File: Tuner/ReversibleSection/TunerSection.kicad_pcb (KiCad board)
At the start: 2 copper layers, 100 x 100 mm, 80 parts, among them J1 Conn_01x03, J10 Conn_01x02, J11 Conn_01x05, J12 Conn_01x01, J13 Conn_01x01, J14 Conn_01x01, J15 Conn_01x01, J2 Conn_01x03, J3 Conn_01x03, J4 Conn_01x03, J5 Conn_01x03, J6 Conn_01x03, J7 Conn_01x03, J8 Conn_01x02, J9 Conn_01x02, P1 Conn_01x01, P10 Conn_01x01, P11 Conn_01x01, P12 Conn_01x01, P2 Conn_01x01, P3 Conn_01x01, P4 Conn_01x01, P5 Conn_01x01, P6 Conn_01x01, P7 Conn_01x01, P8 Conn_01x01, P9 Conn_01x01, U1 MCP23008, U2 ULN2803A

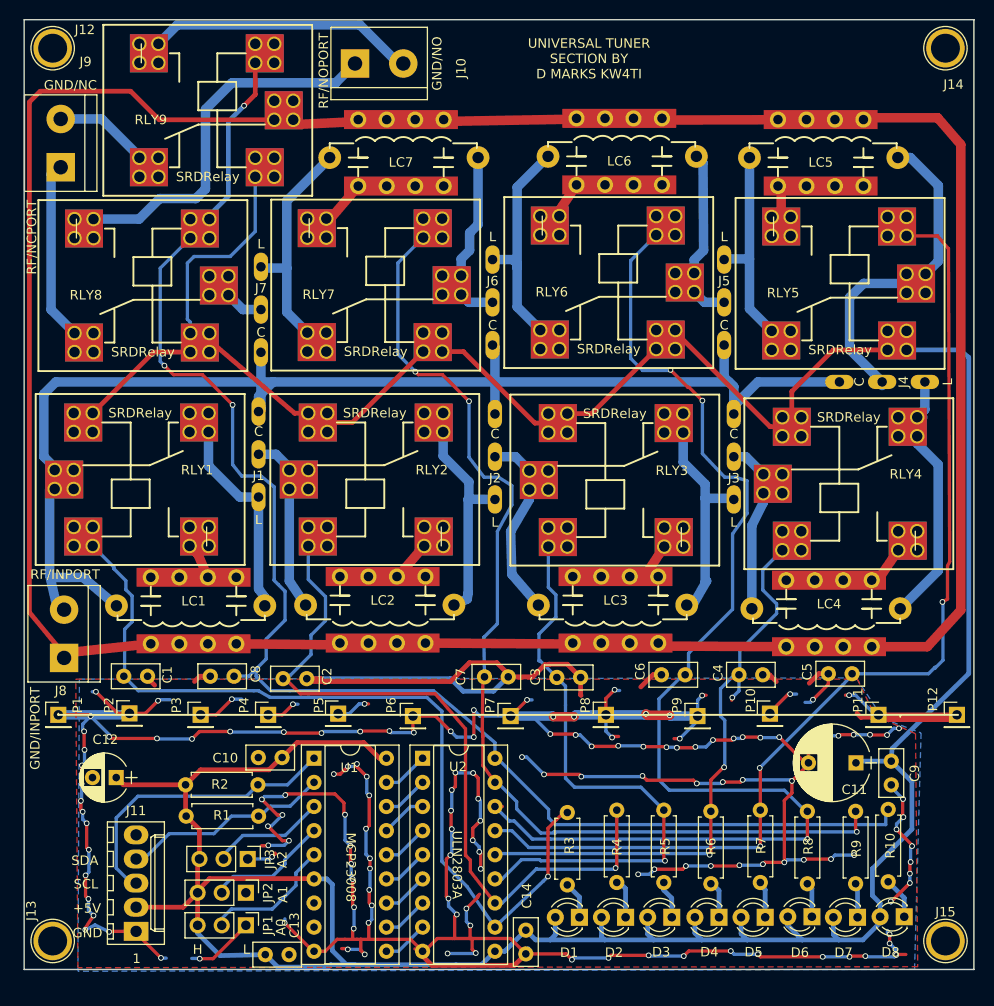
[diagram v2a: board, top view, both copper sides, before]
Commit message: Modified RelayControl and Reversible Section to Isolate Digital from Analog sections using RF chokes
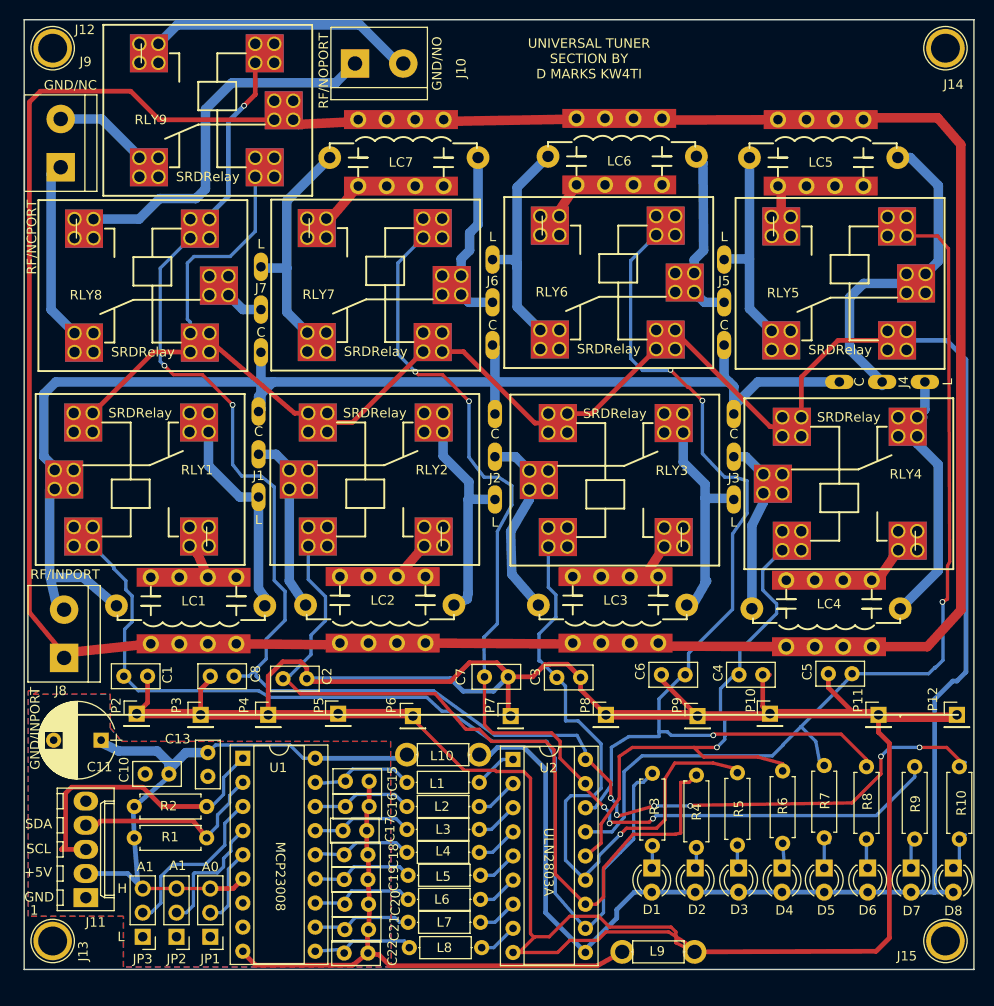
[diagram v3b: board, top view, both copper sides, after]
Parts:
- removed C12: 22 uF, Capacitors_THT:CP_Radial_D5.0mm_P2.50mm
- removed C14, C9: 100 nF, Capacitors_THT:C_Disc_D5.0mm_W2.5mm_P2.50mm
- removed P1: Conn_01x01, Pin_Headers:Pin_Header_Straight_1x01_Pitch2.54mm
- added C15: 10 nF, Capacitors_THT:C_Disc_D5.0mm_W2.5mm_P2.50mm, F.Cu at (83.8, 130.2)
- added C16: C_Small, Capacitors_THT:C_Disc_D5.0mm_W2.5mm_P2.50mm, F.Cu at (83.8, 132.8)
- added C17: C_Small, Capacitors_THT:C_Disc_D5.0mm_W2.5mm_P2.50mm, F.Cu at (83.6, 135.4)
- added C18: 10 nF, Capacitors_THT:C_Disc_D5.0mm_W2.5mm_P2.50mm, F.Cu at (83.7, 137.9)
- added C19: 10 nF, Capacitors_THT:C_Disc_D5.0mm_W2.5mm_P2.50mm, F.Cu at (83.7, 140.5)
- added C20: 10 nF, Capacitors_THT:C_Disc_D5.0mm_W2.5mm_P2.50mm, F.Cu at (83.8, 143.1)
- added C21: 10 nF, Capacitors_THT:C_Disc_D5.0mm_W2.5mm_P2.50mm, F.Cu at (83.8, 145.8)
- added C22: 10 nFl, Capacitors_THT:C_Disc_D5.0mm_W2.5mm_P2.50mm, F.Cu at (83.7, 148.3)
- added L1: 100 uH, Inductors_THT:L_Axial_L5.3mm_D2.2mm_P7.62mm_Horizontal_Vishay_IM-1, F.Cu at (90.3, 130.3)
- added L10: 100 uH, Inductors_THT:L_Axial_L5.3mm_D2.2mm_P7.62mm_Horizontal_Vishay_IM-1, F.Cu at (90.3, 127.4)
- added L2: 100 uH, Inductors_THT:L_Axial_L5.3mm_D2.2mm_P7.62mm_Horizontal_Vishay_IM-1, F.Cu at (90.3, 132.8)
- added L3: 100 uH, Inductors_THT:L_Axial_L5.3mm_D2.2mm_P7.62mm_Horizontal_Vishay_IM-1, F.Cu at (90.3, 135.3)
- added L4: 100 uH, Inductors_THT:L_Axial_L5.3mm_D2.2mm_P7.62mm_Horizontal_Vishay_IM-1, F.Cu at (90.3, 137.7)
- added L5: 100 uH, Inductors_THT:L_Axial_L5.3mm_D2.2mm_P7.62mm_Horizontal_Vishay_IM-1, F.Cu at (90.4, 140.1)
- added L6: 100 uH, Inductors_THT:L_Axial_L5.3mm_D2.2mm_P7.62mm_Horizontal_Vishay_IM-1, F.Cu at (90.4, 142.6)
- added L7: 100 uH, Inductors_THT:L_Axial_L5.3mm_D2.2mm_P7.62mm_Horizontal_Vishay_IM-1, F.Cu at (90.4, 145.0)
- added L8: 100 uH, Inductors_THT:L_Axial_L5.3mm_D2.2mm_P7.62mm_Horizontal_Vishay_IM-1, F.Cu at (90.6, 147.7)
- added L9: 100 uH, Inductors_THT:L_Axial_L5.3mm_D2.2mm_P7.62mm_Horizontal_Vishay_IM-1, F.Cu at (113.0, 148.1)
- moved C11 79.5 mm to (58.1, 125.9)
- moved C13 20.6 mm to (69.3, 129.7), turned to 90 degrees
- moved JP3 13.8 mm to (62.5, 146.6), turned to 180 degrees
- moved C10 12.0 mm to (62.7, 129.4)
- moved R3 9.86 mm to (116.1, 137.0)
- moved U2 9.53 mm to (101.5, 127.9)
- moved D1 9.21 mm to (116.1, 139.3), turned to 270 degrees
- moved R4 9.16 mm to (120.8, 137.2)
- moved D2 8.98 mm to (120.7, 139.3), turned to 270 degrees
- moved D3 8.74 mm to (125.2, 139.3), turned to 270 degrees
- moved R10 8.74 mm to (148.5, 136.3)
- moved R5 8.69 mm to (125.1, 136.9)
- moved R6 8.67 mm to (129.9, 136.7)
- moved JP2 8.65 mm to (66.0, 146.6), turned to 180 degrees
- moved D4 8.42 mm to (129.8, 139.3), turned to 270 degrees
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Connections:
- C1 pad 1: GND -> RLYGND
- C2 pad 1: GND -> RLYGND
- C3 pad 1: GND -> RLYGND
- C4 pad 1: GND -> RLYGND
- C5 pad 1: GND -> RLYGND
- C6 pad 1: GND -> RLYGND
- C7 pad 1: GND -> RLYGND
- C8 pad 1: GND -> RLYGND
- D1 pad 2: +5V -> RLYPWR
- D2 pad 2: +5V -> RLYPWR
- D3 pad 2: +5V -> RLYPWR
- D4 pad 2: +5V -> RLYPWR
- D5 pad 2: +5V -> RLYPWR
- D6 pad 2: +5V -> RLYPWR
- D7 pad 2: +5V -> RLYPWR
- D8 pad 2: +5V -> RLYPWR
- P10 pad 1: GND -> RLYGND
- P11 pad 1: GND -> RLYGND
- P12 pad 1: GND -> RLYGND
- P2 pad 1: GND -> RLYGND
- P3 pad 1: GND -> RLYGND
- P4 pad 1: GND -> RLYGND
- P5 pad 1: GND -> RLYGND
- P6 pad 1: GND -> RLYGND
- P7 pad 1: GND -> RLYGND
- P8 pad 1: GND -> RLYGND
- P9 pad 1: GND -> RLYGND
- RLY1 pad 4: +5V -> RLYPWR
- RLY2 pad 4: +5V -> RLYPWR
- RLY3 pad 4: +5V -> RLYPWR
- RLY4 pad 4: +5V -> RLYPWR
- RLY5 pad 4: +5V -> RLYPWR
- RLY6 pad 4: +5V -> RLYPWR
- RLY7 pad 4: +5V -> RLYPWR
- RLY8 pad 4: +5V -> RLYPWR
- RLY9 pad 4: +5V -> RLYPWR
- U1 pad 10: Net-(U1-Pad10) -> Net-(C22-Pad1)
- U1 pad 11: Net-(U1-Pad11) -> Net-(C21-Pad1)
- U1 pad 12: Net-(U1-Pad12) -> Net-(C20-Pad1)
- U1 pad 13: Net-(U1-Pad13) -> Net-(C19-Pad1)
- U1 pad 14: Net-(U1-Pad14) -> Net-(C18-Pad1)
- U1 pad 15: Net-(U1-Pad15) -> Net-(C17-Pad1)
- U1 pad 16: Net-(U1-Pad16) -> Net-(C16-Pad1)
- U1 pad 17: Net-(U1-Pad17) -> Net-(C15-Pad1)
- U2 pad 1: Net-(U1-Pad17) -> Net-(L1-Pad2)
- U2 pad 10: +5V -> RLYPWR
- U2 pad 2: Net-(U1-Pad16) -> Net-(L2-Pad2)
- U2 pad 3: Net-(U1-Pad15) -> Net-(L3-Pad2)
- U2 pad 4: Net-(U1-Pad14) -> Net-(L4-Pad2)
- U2 pad 5: Net-(U1-Pad13) -> Net-(L5-Pad2)
- U2 pad 6: Net-(U1-Pad12) -> Net-(L6-Pad2)
- U2 pad 7: Net-(U1-Pad11) -> Net-(L7-Pad2)
- U2 pad 8: Net-(U1-Pad10) -> Net-(L8-Pad2)
- U2 pad 9: GND -> RLYGND
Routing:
- net GND: track 577.1 -> 60.4 mm, vias 146 -> 0
- net +5V: track 378.0 -> 69.1 mm
- net RLYGND: track 0.00 -> 291.9 mm
- net RLYPWR: track 0.00 -> 263.1 mm
- net RLY6: track 125.4 -> 102.8 mm
- net RLY1: track 91.4 -> 103.5 mm, vias 1 -> 0
- net Net-(C22-Pad1): track 0.00 -> 11.1 mm
- net Net-(C15-Pad1): track 0.00 -> 11.1 mm
- net Net-(C20-Pad1): track 0.00 -> 11.1 mm
- net RLY8: track 155.0 -> 166.0 mm, vias 3 -> 9
- net Net-(C19-Pad1): track 0.00 -> 10.8 mm
- net Net-(C17-Pad1): track 0.00 -> 10.8 mm
- net Net-(C16-Pad1): track 0.00 -> 10.8 mm
- net Net-(C21-Pad1): track 0.00 -> 10.7 mm
- net Net-(C18-Pad1): track 0.00 -> 10.7 mm
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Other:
- board text removed: "A2"

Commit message: Added extra filtering and shunt to RF ground
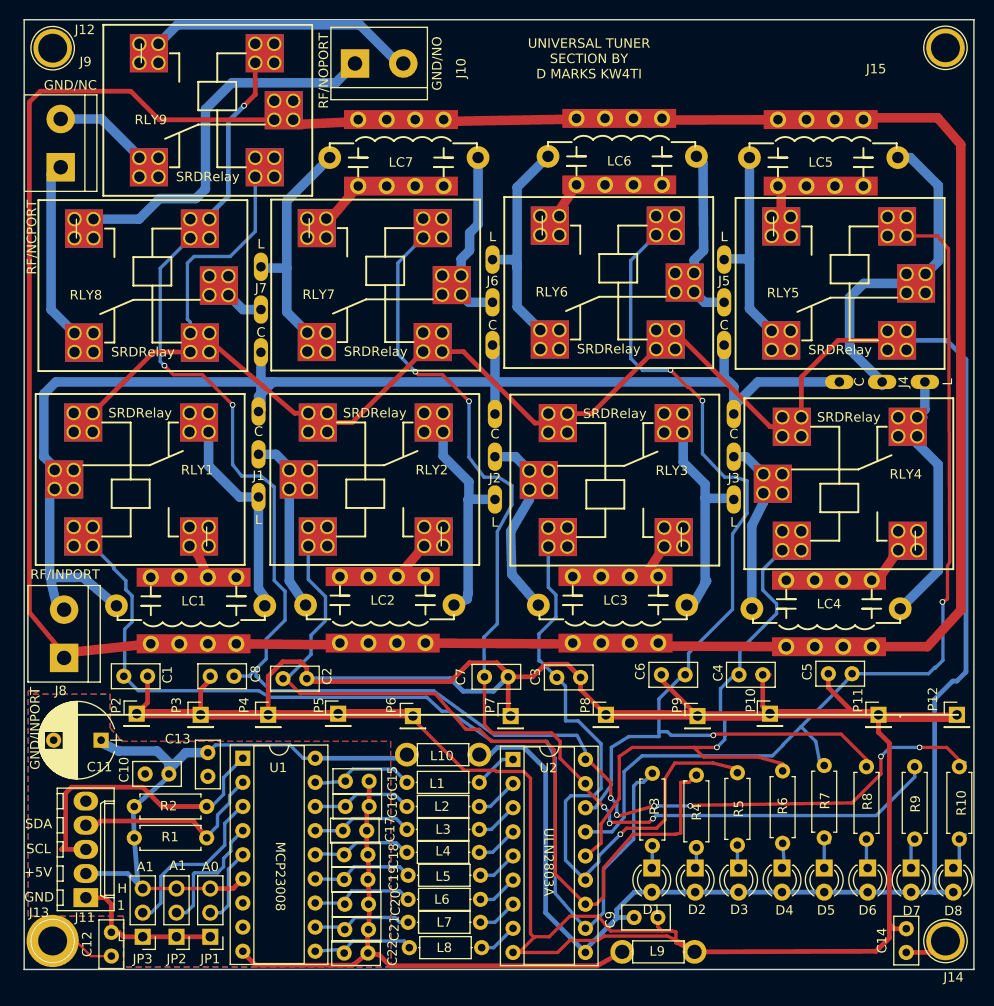
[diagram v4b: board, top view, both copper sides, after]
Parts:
- added C12: 10 nF, Capacitors_THT:C_Disc_D5.0mm_W2.5mm_P2.50mm, F.Cu at (59.2, 148.6)
- added C14: 10 nF, Capacitors_THT:C_Disc_D5.0mm_W2.5mm_P2.50mm, F.Cu at (142.9, 148.2)
- added C9: 10 nF, Capacitors_THT:C_Disc_D5.0mm_W2.5mm_P2.50mm, F.Cu at (114.2, 144.5)
- moved J15 94.0 mm to (147.0, 53.0)
- moved J14 94.0 mm to (147.0, 147.0)
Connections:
- J13 pad 1: (no net) -> Net-(C12-Pad1)
- J14 pad 1: (no net) -> Net-(C14-Pad1)
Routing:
- net GND: track 60.4 -> 77.0 mm
- net Net-(C12-Pad1): track 0.00 -> 6.84 mm
- net Net-(C14-Pad1): track 0.00 -> 4.63 mm
- net RLYGND: track 291.9 -> 295.1 mm
- net RLYPWR: track 263.1 -> 264.9 mm
